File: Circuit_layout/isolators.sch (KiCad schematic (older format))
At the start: 35 parts, among them U17 MCP6004, U19 ACPL-C870, U20 ACPL-C870, U21 MCP6001

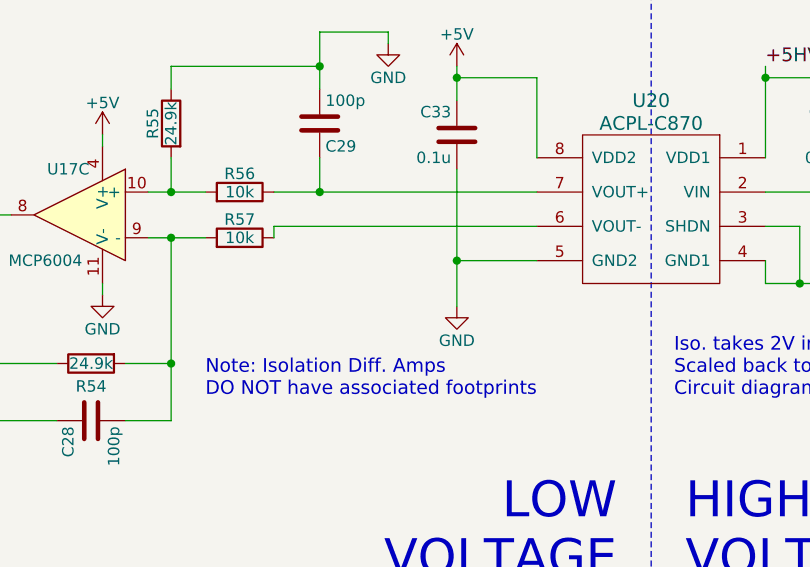
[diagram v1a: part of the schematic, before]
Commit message: cleaned up footprints of more testpoints. ran DRC again, passed
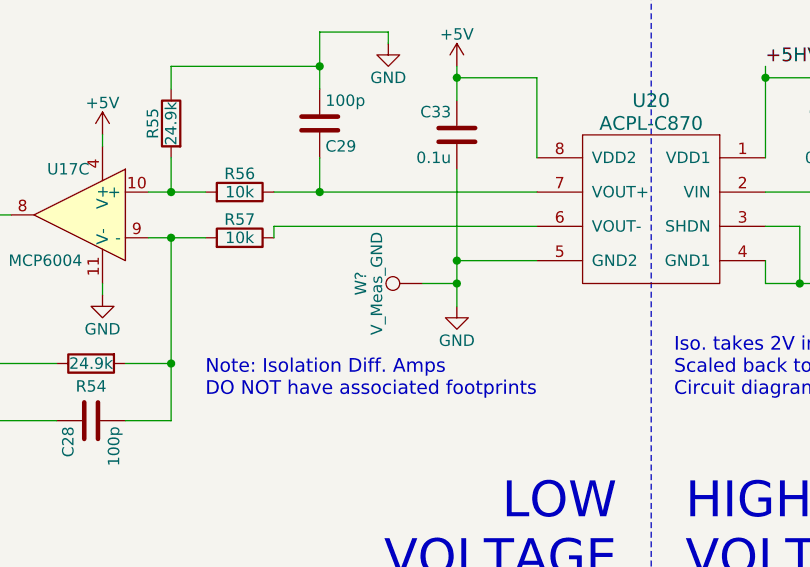
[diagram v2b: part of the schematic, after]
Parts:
- added W?: V_Meas_GND, Measurement_Points:Measurement_Point_Square-SMD-Pad_Big, symbol TEST_1P
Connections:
- net GND: now also W?.1
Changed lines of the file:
@@
 V_Measure
 $Comp
-L GND #PWR0112
+L GND #PWR0110
 U 1 1 58B25770
 P 4950 3100
-F 0 "#PWR0112" H 4950 2850 50  0001 C CNN
+F 0 "#PWR0110" H 4950 2850 50  0001 C CNN
 F 1 "GND" H 4950 2950 50  0000 C CNN
 F 2 "" H 4950 3100 50  0000 C CNN
@@
 $EndComp
 $Comp
-L +5V #PWR0113
+L +5V #PWR0111
 U 1 1 58B257CF
 P 4950 2050
-F 0 "#PWR0113" H 4950 1900 50  0001 C CNN
+F 0 "#PWR0111" H 4950 1900 50  0001 C CNN
 F 1 "+5V" H 4950 2190 50  0000 C CNN
 F 2 "" H 4950 2050 50  0000 C CNN
@@
 +5HV
 $Comp
-L GND #PWR0114
+L GND #PWR0112
 U 1 1 58BC957F
 P 4600 5150
-F 0 "#PWR0114" H 4600 4900 50  0001 C CNN
+F 0 "#PWR0112" H 4600 4900 50  0001 C CNN
 F 1 "GND" H 4600 5000 50  0000 C CNN
 F 2 "" H 4600 5150 50  0000 C CNN
@@
 $EndComp
 $Comp
-L +5V #PWR0115
+L +5V #PWR0113
 U 1 1 58BC9585
 P 4600 4100
-F 0 "#PWR0115" H 4600 3950 50  0001 C CNN
+F 0 "#PWR0113" H 4600 3950 50  0001 C CNN
 F 1 "+5V" H 4600 4240 50  0000 C CNN
 F 2 "" H 4600 4100 50  0000 C CNN
@@
 $EndComp
 $Comp
-L +5V #PWR0116
+L +5V #PWR0114
 U 1 1 58BCCFD7
 P 3050 4400
-F 0 "#PWR0116" H 3050 4250 50  0001 C CNN
+F 0 "#PWR0114" H 3050 4250 50  0001 C CNN
 F 1 "+5V" H 3050 4540 50  0000 C CNN
 F 2 "" H 3050 4400 50  0000 C CNN
@@
 	4300 3950 4300 4000
 $Comp
-L +5V #PWR0117
+L +5V #PWR0115
 U 1 1 58BCDEB7
 P 1400 4450
-F 0 "#PWR0117" H 1400 4300 50  0001 C CNN
+F 0 "#PWR0115" H 1400 4300 50  0001 C CNN
 F 1 "+5V" H 1400 4590 50  0000 C CNN
 F 2 "" H 1400 4450 50  0000 C CNN
@@
 $EndComp
 $Comp
-L GND #PWR0118
+L GND #PWR0116
 U 1 1 58BCDF52
 P 1400 5100
-F 0 "#PWR0118" H 1400 4850 50  0001 C CNN
+F 0 "#PWR0116" H 1400 4850 50  0001 C CNN
 F 1 "GND" H 1400 4950 50  0000 C CNN
 F 2 "" H 1400 5100 50  0000 C CNN
@@
 Connection ~ 2300 4750
 $Comp
-L GND #PWR0119
+L GND #PWR0117
 U 1 1 58D08937
 P 4300 4000
-F 0 "#PWR0119" H 4300 3750 50  0001 C CNN
+F 0 "#PWR0117" H 4300 3750 50  0001 C CNN
 F 1 "GND" H 4300 3850 50  0000 C CNN
 F 2 "" H 4300 4000 50  0000 C CNN
@@
 	3050 5050 3050 5100
 $Comp
-L GND #PWR0120
+L GND #PWR0118
 U 1 1 58D09DC0
 P 3050 5100
-F 0 "#PWR0120" H 3050 4850 50  0001 C CNN
+F 0 "#PWR0118" H 3050 4850 50  0001 C CNN
 F 1 "GND" H 3050 4950 50  0000 C CNN
 F 2 "" H 3050 5100 50  0000 C CNN
@@
 	4950 4950 4600 4950
 Connection ~ 4600 4950
+Wire Wire Line
+	4450 5050 4600 5050
+Connection ~ 4600 5050
+$Comp
+L TEST_1P W?
+U 1 1 58D30357
+P 4450 5050
+F 0 "W?" H 4450 5320 50  0000 C CNN
+F 1 "V_Meas_GND" H 4450 5250 50  0000 C CNN
+F 2 "Measurement_Points:Measurement_Point_Square-SMD-Pad_Big" H 4650 5050 50  0001 C CNN
+F 3 "" H 4650 5050 50  0000 C CNN
+	1    4450 5050
+	0    -1   -1   0
+$EndComp
 $EndSCHEMATC

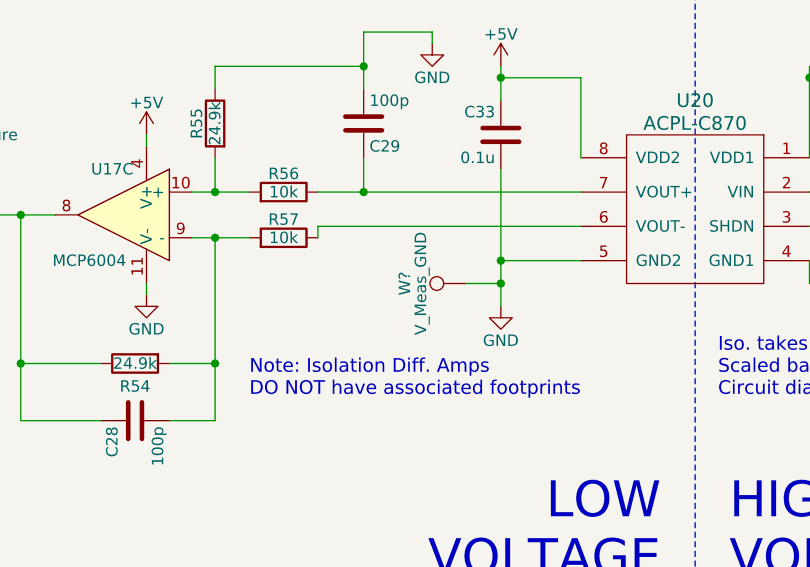
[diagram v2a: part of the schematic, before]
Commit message: started working on throttle layout in pcb. added ch_gnd plane
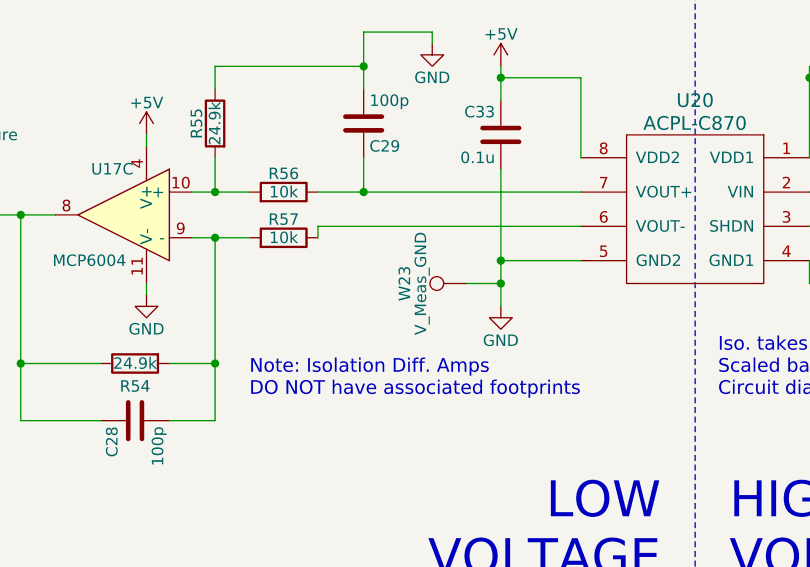
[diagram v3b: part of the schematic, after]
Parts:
- gave numbers to parts that had none: 1
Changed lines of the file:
@@
 V_Measure
 $Comp
-L GND #PWR0110
+L GND #PWR0108
 U 1 1 58B25770
 P 4950 3100
-F 0 "#PWR0110" H 4950 2850 50  0001 C CNN
+F 0 "#PWR0108" H 4950 2850 50  0001 C CNN
 F 1 "GND" H 4950 2950 50  0000 C CNN
 F 2 "" H 4950 3100 50  0000 C CNN
@@
 $EndComp
 $Comp
-L +5V #PWR0111
+L +5V #PWR0109
 U 1 1 58B257CF
 P 4950 2050
-F 0 "#PWR0111" H 4950 1900 50  0001 C CNN
+F 0 "#PWR0109" H 4950 1900 50  0001 C CNN
 F 1 "+5V" H 4950 2190 50  0000 C CNN
 F 2 "" H 4950 2050 50  0000 C CNN
@@
 +5HV
 $Comp
-L GND #PWR0112
+L GND #PWR0110
 U 1 1 58BC957F
 P 4600 5150
-F 0 "#PWR0112" H 4600 4900 50  0001 C CNN
+F 0 "#PWR0110" H 4600 4900 50  0001 C CNN
 F 1 "GND" H 4600 5000 50  0000 C CNN
 F 2 "" H 4600 5150 50  0000 C CNN
@@
 $EndComp
 $Comp
-L +5V #PWR0113
+L +5V #PWR0111
 U 1 1 58BC9585
 P 4600 4100
-F 0 "#PWR0113" H 4600 3950 50  0001 C CNN
+F 0 "#PWR0111" H 4600 3950 50  0001 C CNN
 F 1 "+5V" H 4600 4240 50  0000 C CNN
 F 2 "" H 4600 4100 50  0000 C CNN
@@
 $EndComp
 $Comp
-L +5V #PWR0114
+L +5V #PWR0112
 U 1 1 58BCCFD7
 P 3050 4400
-F 0 "#PWR0114" H 3050 4250 50  0001 C CNN
+F 0 "#PWR0112" H 3050 4250 50  0001 C CNN
 F 1 "+5V" H 3050 4540 50  0000 C CNN
 F 2 "" H 3050 4400 50  0000 C CNN
@@
 	4300 3950 4300 4000
 $Comp
-L +5V #PWR0115
+L +5V #PWR0113
 U 1 1 58BCDEB7
 P 1400 4450
-F 0 "#PWR0115" H 1400 4300 50  0001 C CNN
+F 0 "#PWR0113" H 1400 4300 50  0001 C CNN
 F 1 "+5V" H 1400 4590 50  0000 C CNN
 F 2 "" H 1400 4450 50  0000 C CNN
@@
 $EndComp
 $Comp
-L GND #PWR0116
+L GND #PWR0114
 U 1 1 58BCDF52
 P 1400 5100
-F 0 "#PWR0116" H 1400 4850 50  0001 C CNN
+F 0 "#PWR0114" H 1400 4850 50  0001 C CNN
 F 1 "GND" H 1400 4950 50  0000 C CNN
 F 2 "" H 1400 5100 50  0000 C CNN
@@
 Connection ~ 2300 4750
 $Comp
-L GND #PWR0117
+L GND #PWR0115
 U 1 1 58D08937
 P 4300 4000
-F 0 "#PWR0117" H 4300 3750 50  0001 C CNN
+F 0 "#PWR0115" H 4300 3750 50  0001 C CNN
 F 1 "GND" H 4300 3850 50  0000 C CNN
 F 2 "" H 4300 4000 50  0000 C CNN
@@
 	3050 5050 3050 5100
 $Comp
-L GND #PWR0118
+L GND #PWR0116
 U 1 1 58D09DC0
 P 3050 5100
-F 0 "#PWR0118" H 3050 4850 50  0001 C CNN
+F 0 "#PWR0116" H 3050 4850 50  0001 C CNN
 F 1 "GND" H 3050 4950 50  0000 C CNN
 F 2 "" H 3050 5100 50  0000 C CNN
@@
 Connection ~ 4600 5050
 $Comp
-L TEST_1P W?
+L TEST_1P W23
 U 1 1 58D30357
 P 4450 5050
-F 0 "W?" H 4450 5320 50  0000 C CNN
+F 0 "W23" H 4450 5320 50  0000 C CNN
 F 1 "V_Meas_GND" H 4450 5250 50  0000 C CNN
 F 2 "Measurement_Points:Measurement_Point_Square-SMD-Pad_Big" H 4650 5050 50  0001 C CNN

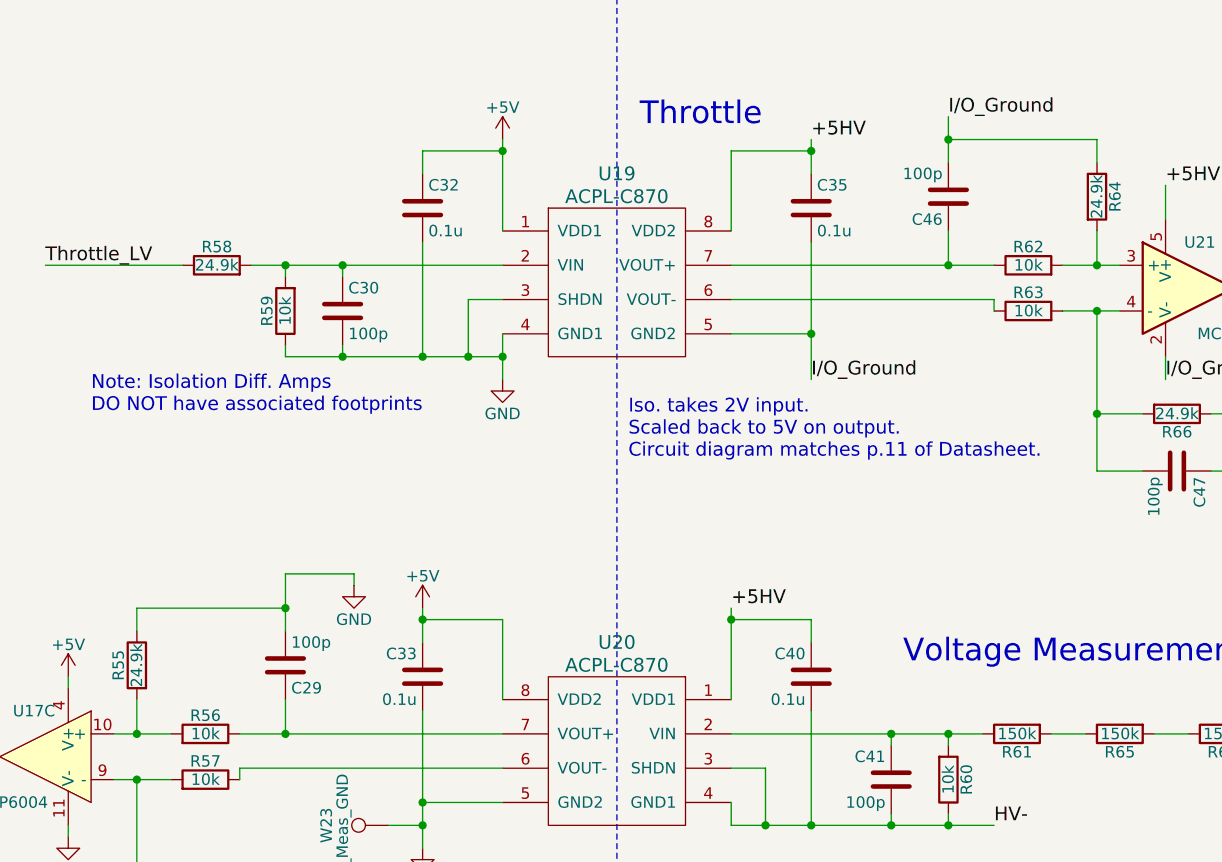
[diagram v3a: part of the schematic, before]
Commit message: reviewed schematic w/ prof. nadovich. proposed changes
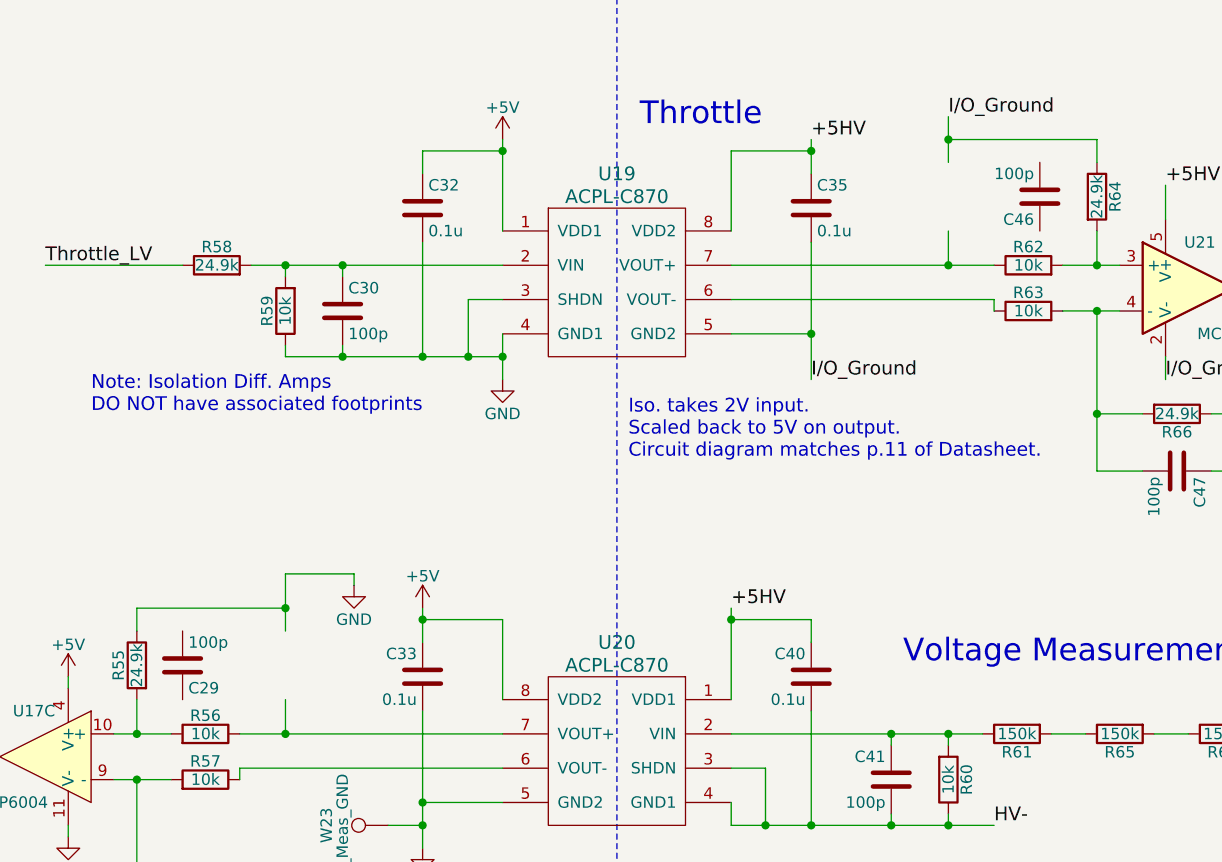
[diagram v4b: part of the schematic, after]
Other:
- moved on the sheet: C29, C46
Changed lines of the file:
@@
 L C C46
 U 1 1 58BC8003
-P 6900 2300
-F 0 "C46" H 6925 2400 50  0000 L CNN
-F 1 "100p" H 6925 2200 50  0000 L CNN
-F 2 "Capacitors_SMD:C_0805_HandSoldering" H 6938 2150 50  0001 C CNN
-F 3 "" H 6900 2300 50  0000 C CNN
-F 4 "399-1122-1-ND" H 6900 2300 60  0001 C CNN "DigiKey P/N"
-F 5 "http://www.digikey.com/product-detail/en/kemet/C0805C101J5GACTU/399-1122-1-ND/411397" H 6900 2300 60  0001 C CNN "URL"
-F 6 "C0805C101J5GACTU" H 6900 2300 60  0001 C CNN "Man P/N"
-	1    6900 2300
+P 7300 2300
+F 0 "C46" H 7325 2400 50  0000 L CNN
+F 1 "100p" H 7325 2200 50  0000 L CNN
+F 2 "Capacitors_SMD:C_0805_HandSoldering" H 7338 2150 50  0001 C CNN
+F 3 "" H 7300 2300 50  0000 C CNN
+F 4 "399-1122-1-ND" H 7300 2300 60  0001 C CNN "DigiKey P/N"
+F 5 "http://www.digikey.com/product-detail/en/kemet/C0805C101J5GACTU/399-1122-1-ND/411397" H 7300 2300 60  0001 C CNN "URL"
+F 6 "C0805C101J5GACTU" H 7300 2300 60  0001 C CNN "Man P/N"
+	1    7300 2300
 	-1   0    0    1
 $EndComp
@@
 L C C29
 U 1 1 58BC963A
-P 4000 4350
-F 0 "C29" H 4025 4450 50  0000 L CNN
-F 1 "100p" H 4025 4250 50  0000 L CNN
-F 2 "Capacitors_SMD:C_0805_HandSoldering" H 4038 4200 50  0001 C CNN
-F 3 "" H 4000 4350 50  0000 C CNN
-F 4 "399-1122-1-ND" H 4000 4350 60  0001 C CNN "DigiKey P/N"
-F 5 "http://www.digikey.com/product-detail/en/kemet/C0805C101J5GACTU/399-1122-1-ND/411397" H 4000 4350 60  0001 C CNN "URL"
-F 6 "C0805C101J5GACTU" H 4000 4350 60  0001 C CNN "Man P/N"
-	1    4000 4350
+P 3550 4350
+F 0 "C29" H 3575 4450 50  0000 L CNN
+F 1 "100p" H 3575 4250 50  0000 L CNN
+F 2 "Capacitors_SMD:C_0805_HandSoldering" H 3588 4200 50  0001 C CNN
+F 3 "" H 3550 4350 50  0000 C CNN
+F 4 "399-1122-1-ND" H 3550 4350 60  0001 C CNN "DigiKey P/N"
+F 5 "http://www.digikey.com/product-detail/en/kemet/C0805C101J5GACTU/399-1122-1-ND/411397" H 3550 4350 60  0001 C CNN "URL"
+F 6 "C0805C101J5GACTU" H 3550 4350 60  0001 C CNN "Man P/N"
+	1    3550 4350
 	1    0    0    1
 $EndComp
